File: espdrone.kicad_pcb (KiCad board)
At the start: 6 copper layers, 55 x 55 mm, 517 parts, among them J1 Conn_02x03_Odd_Even, J10 Conn_01x04_Pin, J11 Conn_01x04_Pin, J2 Conn_01x02, J3 Conn_01x14, J4 Conn_Coaxial, J5 Conn_01x04_Pin, J6 Conn_01x04, J7 Conn_01x06, J8 Conn_01x04_Pin, J9 Conn_01x04_Pin, Q1 NMOS, Q10 PSMN1R4-40YLDX, Q11 PSMN1R4-40YLDX, Q12 PSMN1R4-40YLDX, Q13 PSMN1R4-40YLDX, Q14 PSMN1R4-40YLDX, Q15 PSMN1R4-40YLDX, Q16 PSMN1R4-40YLDX, Q17 PSMN1R4-40YLDX, Q18 PSMN1R4-40YLDX, Q19 PSMN1R4-40YLDX, Q2 NMOS, Q20 PSMN1R4-40YLDX, Q21 PSMN1R4-40YLDX, Q22 PSMN1R4-40YLDX, Q23 PSMN1R4-40YLDX, Q24 PSMN1R4-40YLDX, Q25 PSMN1R4-40YLDX, Q26 PSMN1R4-40YLDX, Q27 PSMN1R4-40YLDX, Q28 PSMN1R4-40YLDX, Q3 NMOS, Q4 NMOS, Q5 PSMN1R4-40YLDX, Q6 PSMN1R4-40YLDX, Q7 PSMN1R4-40YLDX, Q8 PSMN1R4-40YLDX, Q9 PSMN1R4-40YLDX, U10 INA180A2, U11 FPC-1.0FX-15PWCR-H20, U12 VL53L1CXV0FY1, U13 LIS2MDL, U14 LSM6DS3, U15 PMW3901MB-TXQT_C43496881, U16 STM32G071K8U6, U17 DRV8328ARUYR, U18 INA180A2, U19 STM32G071K8U6, U2 USBLC6-2P6, U20 DRV8328ARUYR, U21 INA180A2, U22 STM32G071K8U6, U23 DRV8328ARUYR, U24 INA180A2, U25 STM32G071K8U6, U26 DRV8328ARUYR, U27 INA180A2, U3 W25Q128JVP, U4 LFD182G45DCHD277, U5 ESP32-C5HF4, U6 TLV62569DBV, U7 XC6206P182MR_C347373, U8 TPS63070RNMR, U9 TPS2121RUXR, Y1 Crystal_GND24, Y2 Crystal_GND24

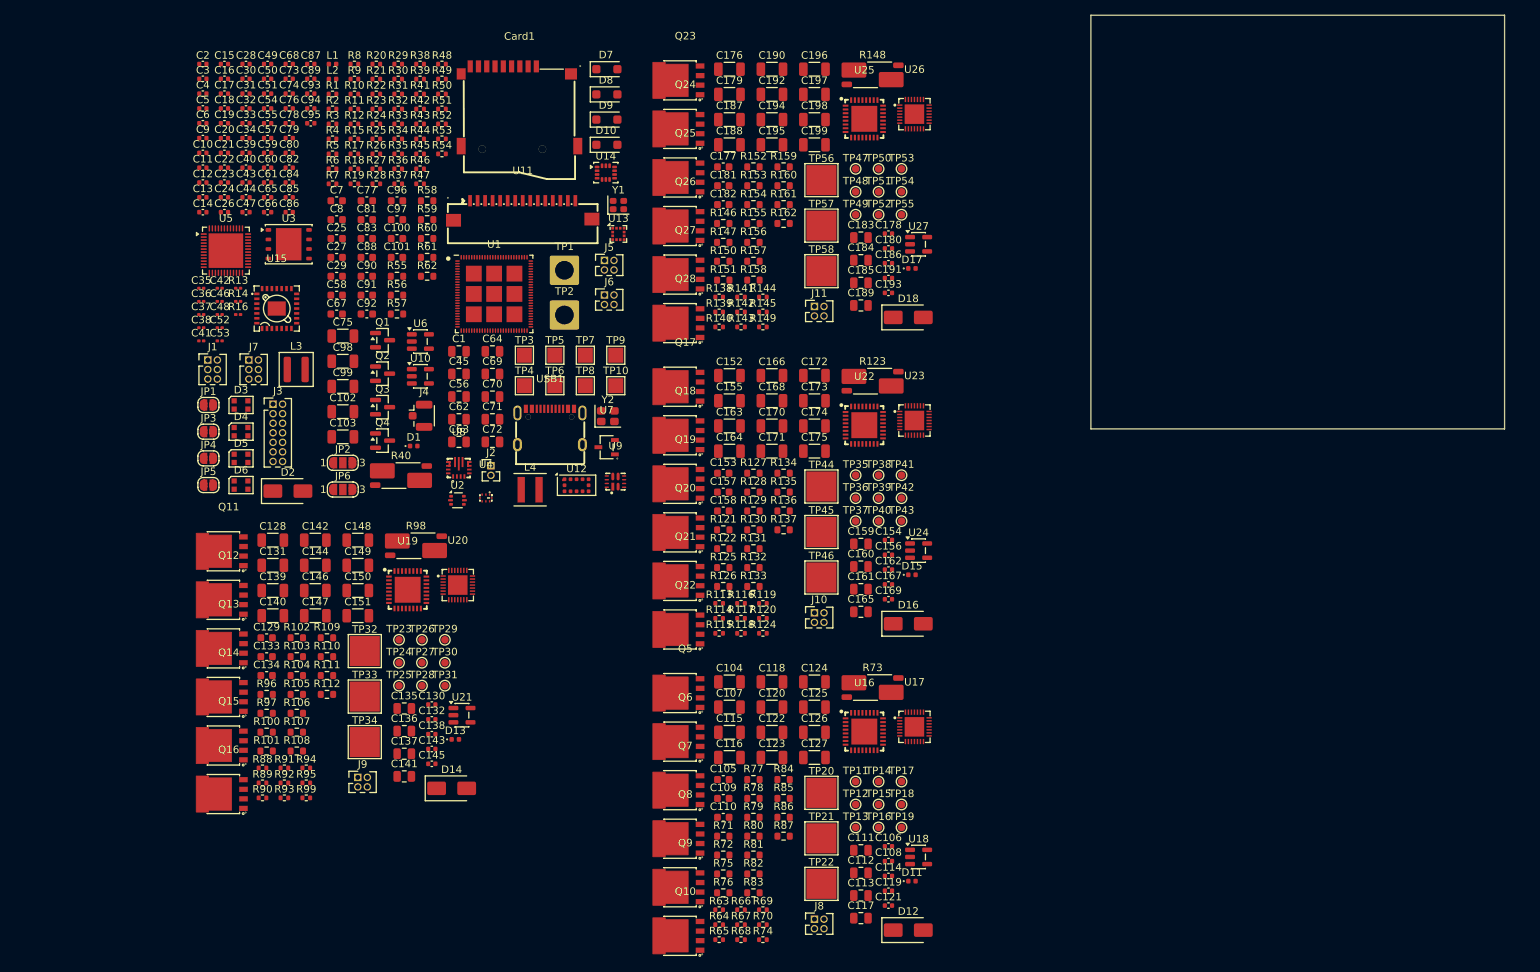
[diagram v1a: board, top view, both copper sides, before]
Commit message: Remove whole battery current shunt and replace MOSFETs with 3.3x3.3mm alternative
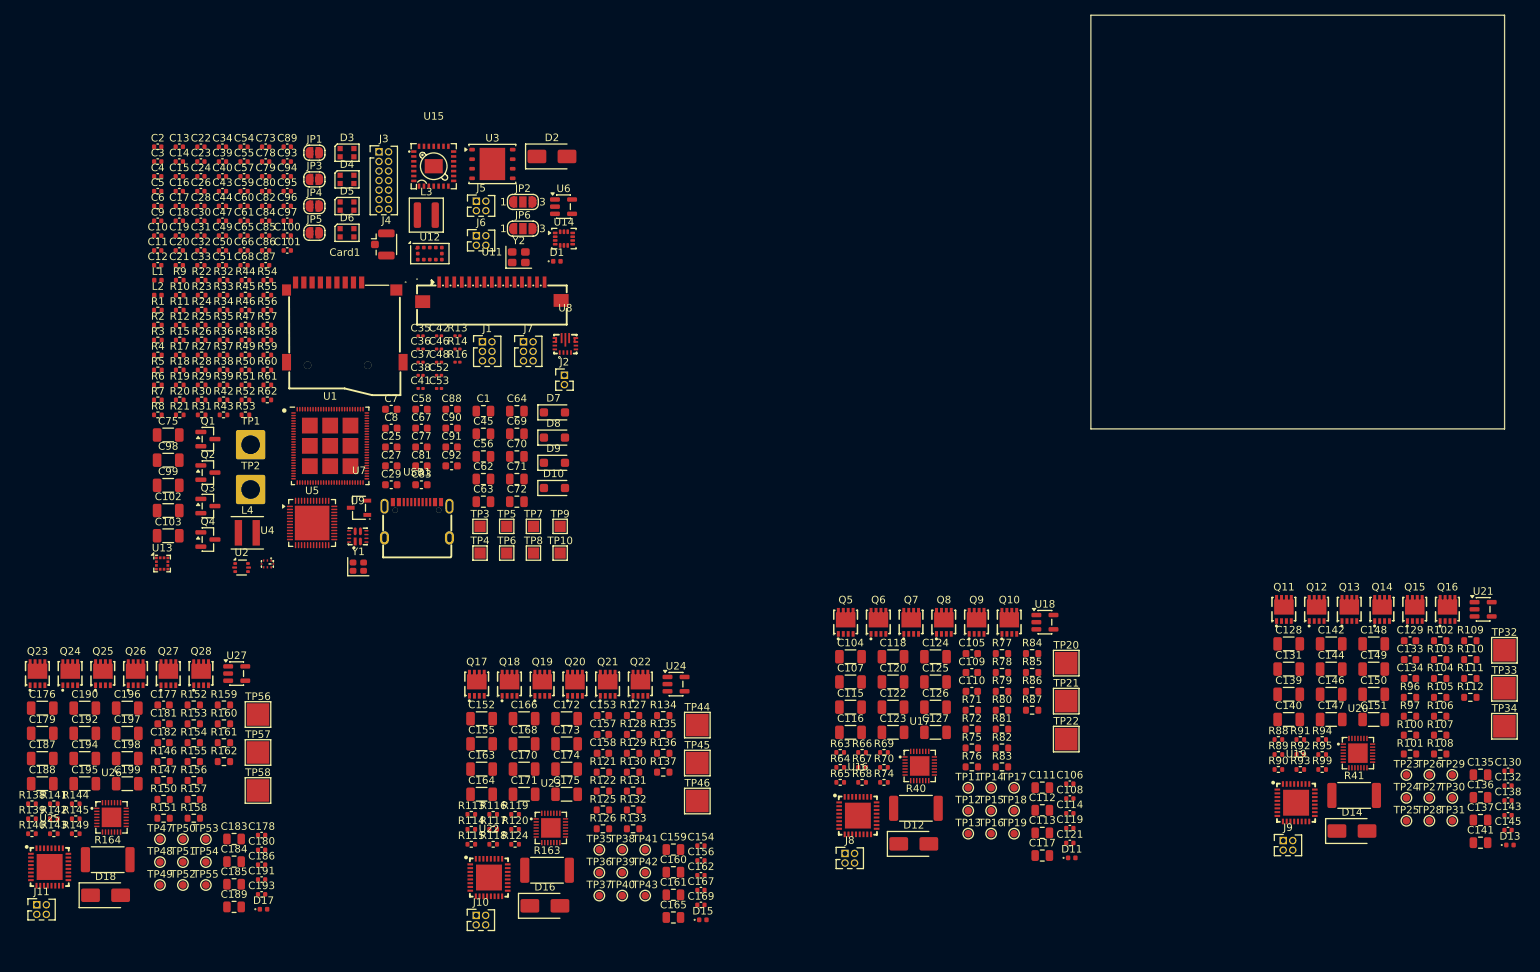
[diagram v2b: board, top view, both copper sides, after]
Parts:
- removed C74: 1n, Capacitor_SMD:C_0402_1005Metric
- removed C76: 100n, Capacitor_SMD:C_0402_1005Metric
- removed R123, R148, R73, R98: 0.001, Resistor_SMD:R_Shunt_Vishay_WSK2512_6332Metric_T2.66mm
- removed U10: INA180A2, Package_TO_SOT_SMD:SOT-23-5
- added R163: 0.001, Resistor_SMD:R_2512_6332Metric, F.Cu at (99.7, 147.7)
- added R164: 0.001, Resistor_SMD:R_2512_6332Metric, F.Cu at (41.3, 146.3)
- C100, C101, C96, C97: footprint Capacitor_SMD:C_0603_1608Metric -> Capacitor_SMD:C_0402_1005Metric
- Q10, Q11, Q12, Q13, Q14, Q15, Q16, Q17, Q18, Q19, Q20, Q21, Q22, Q23, Q24, Q25, Q26, Q27, Q28, Q5, Q6, Q7, Q8, Q9: value PSMN1R4-40YLDX -> NMOS; footprint easyeda2kicad:SOT-669_L4.9-W4.0-P1.27-LS6.0-BR -> easyeda2kicad:PDFN3333-8_L3.1-W3.2-P0.65-LS3.4-BL
- R100, R125, R150, R75: value 10k -> 10
- R101, R126, R151, R76: value 1k -> 10
- R102, R127, R152, R77: value 10 -> 10k
- R103, R128, R153, R78: value 10 -> 1k
- R40: value 0.0005 -> 0.001; footprint Resistor_SMD:R_Shunt_Vishay_WSK2512_6332Metric_T2.66mm -> Resistor_SMD:R_2512_6332Metric
- R41: value 1k -> 0.001; footprint Resistor_SMD:R_0402_1005Metric -> Resistor_SMD:R_2512_6332Metric
- R55, R56, R57, R58, R59, R60, R61, R62: footprint Resistor_SMD:R_0603_1608Metric -> Resistor_SMD:R_0402_1005Metric
- TP10, TP3, TP4, TP5, TP6, TP7, TP8, TP9: footprint TestPoint:TestPoint_Pad_2.0x2.0mm -> TestPoint:TestPoint_Pad_1.5x1.5mm
- TP20, TP21, TP22, TP32, TP33, TP34, TP44, TP45, TP46, TP56, TP57, TP58: footprint TestPoint:TestPoint_Pad_4.0x4.0mm -> TestPoint:TestPoint_Pad_3.0x3.0mm
- moved Q16 163.9 mm to (219.4, 113.0)
- moved Q15 158.7 mm to (215.1, 113.0)
- moved R41 155.3 mm to (207.0, 137.7)
- moved Q14 153.8 mm to (210.7, 113.0)
- moved C129 152.0 mm to (214.4, 117.2)
- moved C133 152.0 mm to (214.4, 119.7)
- moved C134 152.0 mm to (214.4, 122.2)
- moved R100 152.0 mm to (214.4, 129.7)
- moved R101 152.0 mm to (214.4, 132.2)
- moved R96 152.0 mm to (214.4, 124.7)
- moved R97 152.0 mm to (214.4, 127.2)
- moved R102 152.0 mm to (218.4, 117.2)
- moved R103 152.0 mm to (218.4, 119.7)
- moved R104 152.0 mm to (218.4, 122.2)
- moved R105 152.0 mm to (218.4, 124.7)
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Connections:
- C75 pad 2: Net-(C75-Pad2) -> +BATT
- Q10 pad 1: /Motors/ESC/LSS -> Net-(Q10-D)
- Q10 pad 2: /Motors/ESC/LSS -> Net-(Q10-G)
- Q11 pad 1: Net-(Q12-D) -> +BATT
- Q11 pad 2: /Motors/ESC1/A -> Net-(Q11-G)
- Q11 pad 3: /Motors/ESC1/A -> Net-(Q11-S)
- Q12 pad 1: /Motors/ESC1/LSS -> Net-(Q11-S)
- Q12 pad 2: /Motors/ESC1/LSS -> Net-(Q12-G)
- Q13 pad 1: Net-(Q14-D) -> +BATT
- Q13 pad 2: /Motors/ESC1/B -> Net-(Q13-G)
- Q13 pad 3: /Motors/ESC1/B -> Net-(Q13-S)
- Q14 pad 1: /Motors/ESC1/LSS -> Net-(Q13-S)
- Q14 pad 2: /Motors/ESC1/LSS -> Net-(Q14-G)
- Q15 pad 1: Net-(Q16-D) -> +BATT
- Q15 pad 2: /Motors/ESC1/C -> Net-(Q15-G)
- Q15 pad 3: /Motors/ESC1/C -> Net-(Q15-S)
- Q16 pad 1: /Motors/ESC1/LSS -> Net-(Q15-S)
- Q16 pad 2: /Motors/ESC1/LSS -> Net-(Q16-G)
- Q17 pad 1: Net-(Q18-D) -> +BATT
- Q17 pad 2: /Motors/ESC2/A -> Net-(Q17-G)
- Q17 pad 3: /Motors/ESC2/A -> Net-(Q17-S)
- Q18 pad 1: /Motors/ESC2/LSS -> Net-(Q17-S)
- Q18 pad 2: /Motors/ESC2/LSS -> Net-(Q18-G)
- Q19 pad 1: Net-(Q20-D) -> +BATT
- Q19 pad 2: /Motors/ESC2/B -> Net-(Q19-G)
- Q19 pad 3: /Motors/ESC2/B -> Net-(Q19-S)
- Q20 pad 1: /Motors/ESC2/LSS -> Net-(Q19-S)
- Q20 pad 2: /Motors/ESC2/LSS -> Net-(Q20-G)
- Q21 pad 1: Net-(Q22-D) -> +BATT
- Q21 pad 2: /Motors/ESC2/C -> Net-(Q21-G)
- Q21 pad 3: /Motors/ESC2/C -> Net-(Q21-S)
- Q22 pad 1: /Motors/ESC2/LSS -> Net-(Q21-S)
- Q22 pad 2: /Motors/ESC2/LSS -> Net-(Q22-G)
- Q23 pad 1: Net-(Q24-D) -> +BATT
- Q23 pad 2: /Motors/ESC3/A -> Net-(Q23-G)
- Q23 pad 3: /Motors/ESC3/A -> Net-(Q23-S)
- Q24 pad 1: /Motors/ESC3/LSS -> Net-(Q23-S)
- Q24 pad 2: /Motors/ESC3/LSS -> Net-(Q24-G)
- Q25 pad 1: Net-(Q26-D) -> +BATT
- Q25 pad 2: /Motors/ESC3/B -> Net-(Q25-G)
- Q25 pad 3: /Motors/ESC3/B -> Net-(Q25-S)
- Q26 pad 1: /Motors/ESC3/LSS -> Net-(Q25-S)
- Q26 pad 2: /Motors/ESC3/LSS -> Net-(Q26-G)
- Q27 pad 1: Net-(Q28-D) -> +BATT
- Q27 pad 2: /Motors/ESC3/C -> Net-(Q27-G)
- Q27 pad 3: /Motors/ESC3/C -> Net-(Q27-S)
- Q28 pad 1: /Motors/ESC3/LSS -> Net-(Q27-S)
- Q28 pad 2: /Motors/ESC3/LSS -> Net-(Q28-G)
- Q5 pad 1: Net-(Q6-D) -> +BATT
- Q5 pad 2: /Motors/ESC/A -> Net-(Q5-G)
- Q5 pad 3: /Motors/ESC/A -> Net-(Q5-S)
- Q6 pad 1: /Motors/ESC/LSS -> Net-(Q5-S)
- Q6 pad 2: /Motors/ESC/LSS -> Net-(Q6-G)
- Q7 pad 1: Net-(Q8-D) -> +BATT
- Q7 pad 2: /Motors/ESC/B -> Net-(Q7-G)
- Q7 pad 3: /Motors/ESC/B -> Net-(Q7-S)
- Q8 pad 1: /Motors/ESC/LSS -> Net-(Q7-S)
- Q8 pad 2: /Motors/ESC/LSS -> Net-(Q8-G)
- Q9 pad 1: Net-(Q10-D) -> +BATT
- Q9 pad 2: /Motors/ESC/C -> Net-(Q9-G)
- Q9 pad 3: /Motors/ESC/C -> Net-(Q10-D)
- R100 pad 1: /Motors/ESC1/VSENSE_A -> Net-(Q13-G)
- R100 pad 2: /Motors/ESC1/VSENSE_REF -> /Motors/ESC1/GHB
- R101 pad 1: GND -> Net-(Q14-G)
- R101 pad 2: /Motors/ESC1/VSENSE_A -> /Motors/ESC1/GLB
- R102 pad 1: Net-(Q13-G) -> /Motors/ESC1/VSENSE_A
- R102 pad 2: /Motors/ESC1/GHB -> /Motors/ESC1/VSENSE_REF
- R103 pad 1: Net-(Q14-G) -> GND
- R103 pad 2: /Motors/ESC1/GLB -> /Motors/ESC1/VSENSE_A
- R125 pad 1: /Motors/ESC2/VSENSE_A -> Net-(Q19-G)
- R125 pad 2: /Motors/ESC2/VSENSE_REF -> /Motors/ESC2/GHB
- R126 pad 1: GND -> Net-(Q20-G)
- R126 pad 2: /Motors/ESC2/VSENSE_A -> /Motors/ESC2/GLB
- R127 pad 1: Net-(Q19-G) -> /Motors/ESC2/VSENSE_A
- R127 pad 2: /Motors/ESC2/GHB -> /Motors/ESC2/VSENSE_REF
- R128 pad 1: Net-(Q20-G) -> GND
- R128 pad 2: /Motors/ESC2/GLB -> /Motors/ESC2/VSENSE_A
- R150 pad 1: /Motors/ESC3/VSENSE_A -> Net-(Q25-G)
- R150 pad 2: /Motors/ESC3/VSENSE_REF -> /Motors/ESC3/GHB
- R151 pad 1: GND -> Net-(Q26-G)
- R151 pad 2: /Motors/ESC3/VSENSE_A -> /Motors/ESC3/GLB
- R152 pad 1: Net-(Q25-G) -> /Motors/ESC3/VSENSE_A
- R152 pad 2: /Motors/ESC3/GHB -> /Motors/ESC3/VSENSE_REF
- R153 pad 1: Net-(Q26-G) -> GND
- R153 pad 2: /Motors/ESC3/GLB -> /Motors/ESC3/VSENSE_A
- R40 pad 1: +BATT -> /Motors/ESC/LSS
- R40 pad 2: Net-(U10--) -> GND
- R41 pad 1: BAT_ISENSE -> /Motors/ESC1/LSS
- R41 pad 2: Net-(R41-Pad2) -> GND
- R75 pad 1: /Motors/ESC/VSENSE_A -> Net-(Q7-G)
- R75 pad 2: /Motors/ESC/VSENSE_REF -> /Motors/ESC/GHB
- R76 pad 1: GND -> Net-(Q8-G)
- R76 pad 2: /Motors/ESC/VSENSE_A -> /Motors/ESC/GLB
- R77 pad 1: Net-(Q7-G) -> /Motors/ESC/VSENSE_A
- R77 pad 2: /Motors/ESC/GHB -> /Motors/ESC/VSENSE_REF
- R78 pad 1: Net-(Q8-G) -> GND
- R78 pad 2: /Motors/ESC/GLB -> /Motors/ESC/VSENSE_A
- TP1 pad 1: Net-(C75-Pad2) -> +BATT
- U18 pad 3: Net-(U18-+) -> /Motors/ESC/LSS
- U18 pad 4: Net-(U18--) -> GND
- U21 pad 3: Net-(U21-+) -> /Motors/ESC1/LSS
- U21 pad 4: Net-(U21--) -> GND
- U24 pad 3: Net-(U24-+) -> /Motors/ESC2/LSS
- U24 pad 4: Net-(U24--) -> GND
- U27 pad 3: Net-(U27-+) -> /Motors/ESC3/LSS
- U27 pad 4: Net-(U27--) -> GND

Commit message: Improve some connector footprints
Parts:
- removed C198, C199: 10u, Capacitor_SMD:C_1206_3216Metric
- removed D15, D17: LED, LED_SMD:LED_0402_1005Metric
- removed D16, D18: SMAJ14A, Diode_SMD:D_SMA
- removed J6: Conn_01x04, Connector_PinHeader_1.27mm:PinHeader_2x02_P1.27mm_Vertical
- removed R161: 1k, Resistor_SMD:R_0603_1608Metric
- removed R162: 10k, Resistor_SMD:R_0603_1608Metric
- removed R163, R164: 0.001, Resistor_SMD:R_2512_6332Metric
- removed U27: INA180A2, Package_TO_SOT_SMD:SOT-23-5
- added C74: 100u, Capacitor_SMD:C_1206_3216Metric, F.Cu at (329.4, 5.06)
- added C76: 100n, Capacitor_SMD:C_0402_1005Metric, F.Cu at (214.2, 28.3)
- added J12: Conn_01x04, easyeda2kicad:Connector_Pad_1.27mm_1x04, F.Cu at (252.8, 67.5)
- added R123: 10, Resistor_SMD:R_0603_1608Metric, F.Cu at (315.1, -26.3)
- added R148: 10, Resistor_SMD:R_0603_1608Metric, F.Cu at (360.1, -25.3)
- added R73: 10, Resistor_SMD:R_0603_1608Metric, F.Cu at (271.6, -27.3)
- added R98: 10, Resistor_SMD:R_0603_1608Metric, F.Cu at (225.0, -28.3)
- added U10: FPC-1.0FX-15PWCR-H20, easyeda2kicad:FPC-SMD_15P-P1.00_XUNPU_FPC-1.0FX-15PWCR-H20, F.Cu at (244.3, 45.6)
- C100, C101, C96, C97: value 100n -> 100u; footprint Capacitor_SMD:C_0402_1005Metric -> Capacitor_SMD:C_1206_3216Metric
- C102: value 100u -> 10u
- C103: value 100u -> 100n; footprint Capacitor_SMD:C_1206_3216Metric -> Capacitor_SMD:C_0603_1608Metric
- C104, C128, C152, C176: value 10u -> 100n; footprint Capacitor_SMD:C_1206_3216Metric -> Capacitor_SMD:C_0402_1005Metric
- C105, C129, C153, C177: value 100n -> 10u; footprint Capacitor_SMD:C_0603_1608Metric -> Capacitor_SMD:C_1206_3216Metric
- C107, C131, C155, C179: value 10u -> 470nF; footprint Capacitor_SMD:C_1206_3216Metric -> Capacitor_SMD:C_0603_1608Metric
- C108, C132, C156, C180, C79: value 100n -> 1u; footprint Capacitor_SMD:C_0402_1005Metric -> Capacitor_SMD:C_0603_1608Metric
- C109, C133, C157, C181: value 470nF -> 1u; footprint Capacitor_SMD:C_0603_1608Metric -> Capacitor_SMD:C_0805_2012Metric
- C110, C134, C158, C182: footprint Capacitor_SMD:C_0603_1608Metric -> Capacitor_SMD:C_0805_2012Metric
- C112, C117, C136, C141, C160, C165, C184, C189: value 1u -> 100n; footprint Capacitor_SMD:C_0805_2012Metric -> Capacitor_SMD:C_0402_1005Metric
- C113, C137, C161, C185: value 1u -> 10u; footprint Capacitor_SMD:C_0805_2012Metric -> Capacitor_SMD:C_1206_3216Metric
- C114, C138, C162, C186: value 100n -> 10u; footprint Capacitor_SMD:C_0402_1005Metric -> Capacitor_SMD:C_1206_3216Metric
- C115, C139, C163, C187: value 10u -> 1u; footprint Capacitor_SMD:C_1206_3216Metric -> Capacitor_SMD:C_0805_2012Metric
- C119, C143, C167, C191: value 100n -> 1n
- C121, C145, C169, C193: value 1n -> 10u; footprint Capacitor_SMD:C_0402_1005Metric -> Capacitor_SMD:C_1206_3216Metric
- C127, C151, C175: value 10u -> 100n; footprint Capacitor_SMD:C_1206_3216Metric -> Capacitor_SMD:C_0603_1608Metric
- C35, C36: value TBD -> 12pF; footprint Capacitor_SMD:C_0201_0603Metric -> Capacitor_SMD:C_0402_1005Metric
- C37, C38, C41: value TBD -> 1u; footprint Capacitor_SMD:C_0201_0603Metric -> Capacitor_SMD:C_0402_1005Metric
- C39: value 12pF -> 10u; footprint Capacitor_SMD:C_0402_1005Metric -> Capacitor_SMD:C_0805_2012Metric
- C40: value 12pF -> 0.8p; footprint Capacitor_SMD:C_0402_1005Metric -> Capacitor_SMD:C_0201_0603Metric
- C42: value TBD -> 0.3p
- C43, C44, C51: value 1u -> 100n
- C45: value 10u -> 1u; footprint Capacitor_SMD:C_0805_2012Metric -> Capacitor_SMD:C_0402_1005Metric
- C46: value 0.8p -> 2.6p
- C47: value 1u -> 3p; footprint Capacitor_SMD:C_0402_1005Metric -> Capacitor_SMD:C_0201_0603Metric
- C48: value 0.3p -> 100n; footprint Capacitor_SMD:C_0201_0603Metric -> Capacitor_SMD:C_0402_1005Metric
- C49: value 100n -> 10n
- C50: value 100n -> 10u; footprint Capacitor_SMD:C_0402_1005Metric -> Capacitor_SMD:C_0805_2012Metric
- C52: value 2.6p -> TBD
- C53: value 3p -> TBD
- C54, C57: value 100n -> TBD; footprint Capacitor_SMD:C_0402_1005Metric -> Capacitor_SMD:C_0201_0603Metric
- C55: value 10n -> TBD; footprint Capacitor_SMD:C_0402_1005Metric -> Capacitor_SMD:C_0201_0603Metric
- C56: value 10u -> TBD; footprint Capacitor_SMD:C_0805_2012Metric -> Capacitor_SMD:C_0201_0603Metric
- C75: value 100u -> 10u; footprint Capacitor_SMD:C_1206_3216Metric -> Capacitor_SMD:C_0603_1608Metric
- C77, C92: value 10u -> 100n; footprint Capacitor_SMD:C_0603_1608Metric -> Capacitor_SMD:C_0402_1005Metric
- C81: value 1u -> 4.7u
- C83: value 4.7u -> 10n; footprint Capacitor_SMD:C_0603_1608Metric -> Capacitor_SMD:C_0402_1005Metric
- C85: value 10n -> 220n
- C86: value 100n -> 10u; footprint Capacitor_SMD:C_0402_1005Metric -> Capacitor_SMD:C_0603_1608Metric
- C87: value 220n -> 100n
- C89: value 100n -> 4.7u; footprint Capacitor_SMD:C_0402_1005Metric -> Capacitor_SMD:C_0603_1608Metric
- C91: value 4.7u -> 100n; footprint Capacitor_SMD:C_0603_1608Metric -> Capacitor_SMD:C_0402_1005Metric
- C98, C99: value 100u -> 100n; footprint Capacitor_SMD:C_1206_3216Metric -> Capacitor_SMD:C_0402_1005Metric
- D12, D14: value SMAJ14A -> LED; footprint Diode_SMD:D_SMA -> LED_SMD:LED_0402_1005Metric
- D2: value SMAJ14A -> SMF14A; footprint Diode_SMD:D_SMA -> Diode_SMD:D_SMF
- J1: value Conn_02x03_Odd_Even -> Conn_01x06; footprint Connector_PinHeader_1.27mm:PinHeader_2x03_P1.27mm_Vertical -> easyeda2kicad:Connector_Pad_1.27mm_1x06
- J10, J11, J8, J9: value Conn_01x04_Pin -> Conn_01x04; footprint Connector_PinHeader_1.27mm:PinHeader_2x02_P1.27mm_Vertical -> easyeda2kicad:Connector_Pad_1.27mm_1x04
- J2: value Conn_01x02 -> Conn_01x04; footprint Connector_PinHeader_1.27mm:PinHeader_1x02_P1.27mm_Vertical -> easyeda2kicad:Connector_Pad_1.27mm_1x04
- J3: footprint Connector_PinHeader_1.27mm:PinHeader_2x07_P1.27mm_Vertical -> easyeda2kicad:Connector_pad_1.27mm_2x07
- J4: value Conn_Coaxial -> Conn_01x06; footprint Connector_Coaxial:U.FL_Hirose_U.FL-R-SMT-1_Vertical -> easyeda2kicad:Connector_Pad_1.27mm_1x06
- J5: value Conn_01x04_Pin -> Conn_Coaxial; footprint Connector_PinHeader_1.27mm:PinHeader_2x02_P1.27mm_Vertical -> Connector_Coaxial:U.FL_Hirose_U.FL-R-SMT-1_Vertical
- J7: footprint Connector_PinHeader_1.27mm:PinHeader_2x03_P1.27mm_Vertical -> easyeda2kicad:Connector_Pad_1.27mm_1x06
- R100, R108, R125, R133, R150, R158, R55, R56, R59, R60, R75, R83: value 10 -> 10k
- R101, R109, R126, R134, R151, R159, R76, R84: value 10 -> 1k
- R103, R116, R128, R141, R153, R66, R78, R91: value 1k -> 10k
- R104, R118, R129, R143, R154, R68, R79, R93: value 10k -> 1k
- R106, R131, R156, R81: value 1k -> 10
- R107, R132, R157, R53, R57, R58, R82: value 10k -> 10
- R111, R136, R86: value 1k -> 4.7k; footprint Resistor_SMD:R_0603_1608Metric -> Resistor_SMD:R_0402_1005Metric
- R112, R137, R87: value 10k -> 4.7k; footprint Resistor_SMD:R_0603_1608Metric -> Resistor_SMD:R_0402_1005Metric
- R113, R138, R63, R88: value 4.7k -> 10k
- R114, R139, R64, R89: value 4.7k -> 1k
- R115, R140, R65, R90: value 10k -> 220k
- R117, R142, R67, R92: value 220k -> 10k
- R119, R144, R69, R94: value 10k -> 10; footprint Resistor_SMD:R_0402_1005Metric -> Resistor_SMD:R_0603_1608Metric
- R120, R124, R145, R149, R70, R74, R95, R99: value 1k -> 10; footprint Resistor_SMD:R_0402_1005Metric -> Resistor_SMD:R_0603_1608Metric
- R121, R146, R71, R96: value 10 -> 0.001; footprint Resistor_SMD:R_0603_1608Metric -> Resistor_SMD:R_2512_6332Metric
- R122, R147, R72, R97: value 10 -> 1k; footprint Resistor_SMD:R_0603_1608Metric -> Resistor_SMD:R_0402_1005Metric
- R13, R14: value 0 -> 10k; footprint Resistor_SMD:R_0201_0603Metric -> Resistor_SMD:R_0402_1005Metric
- R16: value 0 -> 47k; footprint Resistor_SMD:R_0201_0603Metric -> Resistor_SMD:R_0402_1005Metric
- R17, R23, R25: value 10k -> 47k
- R20, R22, R45, R46: value 47k -> 10k
- R26, R28: value 47k -> 0; footprint Resistor_SMD:R_0402_1005Metric -> Resistor_SMD:R_0201_0603Metric
- R27: value 10k -> 0; footprint Resistor_SMD:R_0402_1005Metric -> Resistor_SMD:R_0201_0603Metric
- R40, R41: value 0.001 -> 47k; footprint Resistor_SMD:R_2512_6332Metric -> Resistor_SMD:R_0402_1005Metric
- R52, R61, R62: value 10k -> 4.7k
- R54: value 4.7k -> 10
- TP1, TP2: footprint Connector_Wire:SolderWire-2sqmm_1x01_D2mm_OD3.9mm -> easyeda2kicad:BatteryPad_4x3mm
- TP10, TP3, TP4, TP5, TP6, TP7, TP8, TP9: footprint TestPoint:TestPoint_Pad_1.5x1.5mm -> easyeda2kicad:MotorPad_1x3mm
- TP20, TP21, TP22, TP32, TP33, TP34, TP44, TP45, TP46, TP56, TP57, TP58: footprint TestPoint:TestPoint_Pad_3.0x3.0mm -> easyeda2kicad:MotorPad_1x3mm
- U11: value FPC-1.0FX-15PWCR-H20 -> VL53L1CXV0FY1; footprint easyeda2kicad:FPC-SMD_15P-P1.00_XUNPU_FPC-1.0FX-15PWCR-H20 -> Sensor_Distance:ST_VL53L1x
- U12: value VL53L1CXV0FY1 -> LIS2MDL; footprint Sensor_Distance:ST_VL53L1x -> Package_LGA:LGA-12_2x2mm_P0.5mm
- U13: value LIS2MDL -> LSM6DS3; footprint Package_LGA:LGA-12_2x2mm_P0.5mm -> Package_LGA:LGA-14_3x2.5mm_P0.5mm_LayoutBorder3x4y
- U14: value LSM6DS3 -> PMW3901MB-TXQT_C43496881; footprint Package_LGA:LGA-14_3x2.5mm_P0.5mm_LayoutBorder3x4y -> lcsc_footprints:C43496881_COB-28_L6_0-W6_0-P0_65-TL-EP
- U15: value PMW3901MB-TXQT_C43496881 -> STM32G071K8U6; footprint lcsc_footprints:C43496881_COB-28_L6_0-W6_0-P0_65-TL-EP -> easyeda2kicad:UFQFPN-32_L5.0-W5.0-P0.50-TL-EP3.5
- U16, U19, U22, U25: value STM32G071K8U6 -> DRV8328ARUYR; footprint easyeda2kicad:UFQFPN-32_L5.0-W5.0-P0.50-TL-EP3.5 -> easyeda2kicad:QFN-28_L4.0-W4.0-P0.40-BL-EP2.6
- U17, U20, U23, U26: value DRV8328ARUYR -> INA180A2; footprint easyeda2kicad:QFN-28_L4.0-W4.0-P0.40-BL-EP2.6 -> Package_TO_SOT_SMD:SOT-23-5
- U18, U21, U24: value INA180A2 -> STM32G071K8U6; footprint Package_TO_SOT_SMD:SOT-23-5 -> easyeda2kicad:UFQFPN-32_L5.0-W5.0-P0.50-TL-EP3.5
- U4: value LFD182G45DCHD277 -> ESP32-C5HF4; footprint easyeda2kicad:FILTER-SMD_8P-L1.6-W0.8-LFD182G45DCHD277 -> Package_DFN_QFN:QFN-48-1EP_6x6mm_P0.4mm_EP4.6x4.6mm
- U5: value ESP32-C5HF4 -> LFD182G45DCHD277; footprint Package_DFN_QFN:QFN-48-1EP_6x6mm_P0.4mm_EP4.6x4.6mm -> easyeda2kicad:FILTER-SMD_8P-L1.6-W0.8-LFD182G45DCHD277
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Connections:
- C104 pad 1: +BATT -> GND
- C104 pad 2: GND -> +3V3
- C105 pad 1: +BATT -> /Motors/ESC1/GVDD
- C107 pad 1: /Motors/ESC/GVDD -> Net-(U16-CPL)
- C107 pad 2: GND -> Net-(U16-CPH)
- C109 pad 1: Net-(U17-CPL) -> /Motors/ESC1/A
- C109 pad 2: Net-(U17-CPH) -> /Motors/ESC1/BSTA
- C110 pad 1: GND -> /Motors/ESC1/B
- C110 pad 2: +3V3 -> Net-(U16-BSTB)
- C111 pad 1: /Motors/ESC/A -> /Motors/ESC1/C
- C111 pad 2: /Motors/ESC/BSTA -> Net-(U16-BSTC)
- C112 pad 1: /Motors/ESC/B -> GND
- C112 pad 2: Net-(U17-BSTB) -> +BATT
- C113 pad 1: /Motors/ESC/C -> GND
- C113 pad 2: Net-(U17-BSTC) -> +BATT
- C117 pad 1: GND -> +3V3
- C117 pad 2: +BATT -> GND
- C119 pad 1: +3V3 -> /Motors/ESC1/ISENSE
- C121 pad 1: /Motors/ESC/ISENSE -> GND
- C121 pad 2: GND -> +BATT
- C126 pad 1: GND -> +BATT
- C126 pad 2: +BATT -> GND
- C127 pad 1: GND -> +BATT
- C127 pad 2: +BATT -> GND
- C128 pad 1: +BATT -> GND
- C128 pad 2: GND -> +3V3
- C129 pad 1: +BATT -> /Motors/ESC2/GVDD
- C131 pad 1: /Motors/ESC1/GVDD -> Net-(U19-CPL)
- C131 pad 2: GND -> Net-(U19-CPH)
- C133 pad 1: Net-(U20-CPL) -> /Motors/ESC2/A
- C133 pad 2: Net-(U20-CPH) -> /Motors/ESC2/BSTA
- C134 pad 1: GND -> /Motors/ESC2/B
- C134 pad 2: +3V3 -> Net-(U19-BSTB)
- C135 pad 1: /Motors/ESC1/A -> /Motors/ESC2/C
- C135 pad 2: /Motors/ESC1/BSTA -> Net-(U19-BSTC)
- C136 pad 1: /Motors/ESC1/B -> GND
- C136 pad 2: Net-(U20-BSTB) -> +BATT
- C137 pad 1: /Motors/ESC1/C -> GND
- C137 pad 2: Net-(U20-BSTC) -> +BATT
- C141 pad 1: GND -> +3V3
- C141 pad 2: +BATT -> GND
- C143 pad 1: +3V3 -> /Motors/ESC2/ISENSE
- C145 pad 1: /Motors/ESC1/ISENSE -> GND
- C145 pad 2: GND -> +BATT
- C150 pad 1: GND -> +BATT
- C150 pad 2: +BATT -> GND
- C151 pad 1: GND -> +BATT
- C151 pad 2: +BATT -> GND
- C152 pad 1: +BATT -> GND
- C152 pad 2: GND -> +3V3
- C153 pad 1: +BATT -> /Motors/ESC3/GVDD
- C155 pad 1: /Motors/ESC2/GVDD -> Net-(U22-CPL)
- C155 pad 2: GND -> Net-(U22-CPH)
- C157 pad 1: Net-(U23-CPL) -> /Motors/ESC3/A
- C157 pad 2: Net-(U23-CPH) -> /Motors/ESC3/BSTA
- C158 pad 1: GND -> /Motors/ESC3/B
- C158 pad 2: +3V3 -> Net-(U22-BSTB)
- C159 pad 1: /Motors/ESC2/A -> /Motors/ESC3/C
- C159 pad 2: /Motors/ESC2/BSTA -> Net-(U22-BSTC)
- C160 pad 1: /Motors/ESC2/B -> GND
- C160 pad 2: Net-(U23-BSTB) -> +BATT
- C161 pad 1: /Motors/ESC2/C -> GND
- C161 pad 2: Net-(U23-BSTC) -> +BATT
- C165 pad 1: GND -> +3V3
- C165 pad 2: +BATT -> GND
- C167 pad 1: +3V3 -> /Motors/ESC3/ISENSE
- C169 pad 1: /Motors/ESC2/ISENSE -> GND
- C169 pad 2: GND -> +BATT
- C174 pad 1: GND -> +BATT
- C174 pad 2: +BATT -> GND
- C175 pad 1: GND -> +BATT
- C175 pad 2: +BATT -> GND
- C176 pad 1: +BATT -> GND
- C176 pad 2: GND -> +3V3
- C177 pad 1: +BATT -> /Motors/ESC4/GVDD
- C179 pad 1: /Motors/ESC3/GVDD -> Net-(U25-CPL)
- C179 pad 2: GND -> Net-(U25-CPH)
- C181 pad 1: Net-(U26-CPL) -> /Motors/ESC4/A
- C181 pad 2: Net-(U26-CPH) -> /Motors/ESC4/BSTA
- C182 pad 1: GND -> /Motors/ESC4/B
- C182 pad 2: +3V3 -> Net-(U25-BSTB)
- C183 pad 1: /Motors/ESC3/A -> /Motors/ESC4/C
- C183 pad 2: /Motors/ESC3/BSTA -> Net-(U25-BSTC)
- C184 pad 1: /Motors/ESC3/B -> GND
- C184 pad 2: Net-(U26-BSTB) -> +BATT
- C185 pad 1: /Motors/ESC3/C -> GND
- C185 pad 2: Net-(U26-BSTC) -> +BATT
- C189 pad 1: GND -> +3V3
- C189 pad 2: +BATT -> GND
- C191 pad 1: +3V3 -> /Motors/ESC4/ISENSE
- C193 pad 1: /Motors/ESC3/ISENSE -> GND
- C193 pad 2: GND -> +BATT
- C35 pad 1: /Coprocessor/ANT_5G -> Net-(C35-Pad1)
- C36 pad 1: /Coprocessor/ANT_2G -> Net-(U4-XTAL_N)
- C37 pad 1: Net-(U4-P1) -> CP_EN
- C38 pad 1: Net-(U4-P2) -> +3V3
- C39 pad 1: Net-(C39-Pad1) -> +3V3
- C40 pad 1: Net-(U5-XTAL_N) -> +3V3
- C41 pad 1: Net-(U4-P3) -> +3V3
- C42 pad 1: Net-(J4-In) -> +3V3
- C43 pad 1: CP_EN -> +3V3
- C46 pad 1: +3V3 -> Net-(U4-VDDA1)
- C52 pad 1: Net-(U5-VDDA1) -> /Coprocessor/ANT_5G
- C53 pad 1: +3V3 -> /Coprocessor/ANT_2G
- C54 pad 1: +3V3 -> Net-(U5-P1)
- C55 pad 1: +3V3 -> Net-(U5-P2)
- C56 pad 1: +3V3 -> Net-(U5-P3)
- C57 pad 1: +3V3 -> Net-(J5-In)
- C75 pad 2: +BATT -> +3V3
- C77 pad 1: GND -> +3V3
- C77 pad 2: +3V3 -> GND
- C79 pad 1: +3V3 -> GND
- C79 pad 2: GND -> +3V3
- C82 pad 1: +3V3 -> GND
- C82 pad 2: GND -> +3V3
- C85 pad 2: +3V3 -> Net-(U12-C1)
- C87 pad 2: Net-(U13-C1) -> +3V3
- C88 pad 2: +3V3 -> +1V8
- C89 pad 2: +3V3 -> Net-(U14-VREG)
- C91 pad 2: Net-(U15-VREG) -> Net-(U14-VREG)
- C93 pad 2: Net-(U15-VREG) -> +3V3
- C94 pad 1: GND -> +BATT
- C94 pad 2: +1V8 -> GND
- C95 pad 1: GND -> +BATT
- C95 pad 2: +3V3 -> GND
- D12 pad 2: +BATT -> Net-(D12-A)
- D14 pad 2: +BATT -> Net-(D14-A)
- J1 pad 1: /MCU/P4_MTDO -> GND
- J1 pad 2: +3V3 -> /MCU/P4_MTDO
- J1 pad 3: GND -> /MCU/P4_MTMS
- J1 pad 4: /MCU/P4_MTCK -> /MCU/P4_MTDI
- J1 pad 5: /MCU/P4_MTMS -> /MCU/P4_MTCK
- J1 pad 6: /MCU/P4_MTDI -> +3V3
- J10 pad 1: +3V3 -> GND
- J10 pad 2: /Motors/ESC2/SWDIO -> /Motors/ESC3/SWCLK
- J10 pad 3: /Motors/ESC2/SWCLK -> /Motors/ESC3/SWDIO
- J10 pad 4: GND -> +3V3
- J11 pad 1: +3V3 -> GND
- J11 pad 2: /Motors/ESC3/SWDIO -> /Motors/ESC4/SWCLK
- J11 pad 3: /Motors/ESC3/SWCLK -> /Motors/ESC4/SWDIO
- J11 pad 4: GND -> +3V3
- J2 pad 1: Net-(J2-Pin_1) -> GND
- J3 pad 1: +3V3 -> GND
- J3 pad 10: /MCU/GPIO49 -> /MCU/GPIO30
- J3 pad 11: /MCU/GPIO50 -> /MCU/GPIO29
- J3 pad 12: /MCU/GPIO51 -> /MCU/GPIO28
- J3 pad 13: /MCU/GPIO52 -> /MCU/GPIO6
- J3 pad 14: GND -> +3V3
- J3 pad 2: /MCU/GPIO6 -> /MCU/GPIO52
- J3 pad 3: /MCU/GPIO28 -> /MCU/GPIO51
- J3 pad 4: /MCU/GPIO29 -> /MCU/GPIO50
- J3 pad 5: /MCU/GPIO30 -> /MCU/GPIO49
- J3 pad 6: /MCU/GPIO31 -> /MCU/GPIO34
- J3 pad 7: /MCU/GPIO32 -> /MCU/GPIO33
- J3 pad 8: /MCU/GPIO33 -> /MCU/GPIO32
- J3 pad 9: /MCU/GPIO34 -> /MCU/GPIO31
- J4 pad 1: Net-(J4-In) -> GND
- J4 pad 2: GND -> Net-(J4-Pin_2)
- J5 pad 1: Net-(J5-Pin_1) -> Net-(J5-In)
- J5 pad 2: Net-(J5-Pin_2) -> GND
- J7 pad 1: +3V3 -> GND
- J7 pad 2: SPI_CLK -> SPI_MOSI
- J7 pad 3: SPI_EXT_CS -> SPI_MISO
- J7 pad 4: SPI_MISO -> SPI_EXT_CS
- J7 pad 5: SPI_MOSI -> SPI_CLK
- J7 pad 6: GND -> +3V3
- J8 pad 1: +3V3 -> GND
- J8 pad 2: /Motors/ESC/SWDIO -> /Motors/ESC1/SWCLK
- J8 pad 3: /Motors/ESC/SWCLK -> /Motors/ESC1/SWDIO
- J8 pad 4: GND -> +3V3
- J9 pad 1: +3V3 -> GND
- J9 pad 2: /Motors/ESC1/SWDIO -> /Motors/ESC2/SWCLK
- J9 pad 3: /Motors/ESC1/SWCLK -> /Motors/ESC2/SWDIO
- J9 pad 4: GND -> +3V3
- JP2 pad 2: Net-(J5-Pin_2) -> Net-(J4-Pin_4)
- L1 pad 1: Net-(C39-Pad1) -> Net-(C35-Pad1)
- L1 pad 2: Net-(U5-XTAL_P) -> Net-(U4-XTAL_P)
- L2 pad 2: Net-(U5-VDDA1) -> Net-(U4-VDDA1)
- Q10 pad 3: /Motors/ESC/LSS -> /Motors/ESC1/LSS
- Q12 pad 3: /Motors/ESC1/LSS -> /Motors/ESC2/LSS
- Q14 pad 3: /Motors/ESC1/LSS -> /Motors/ESC2/LSS
- Q16 pad 3: /Motors/ESC1/LSS -> /Motors/ESC2/LSS
- Q18 pad 3: /Motors/ESC2/LSS -> /Motors/ESC3/LSS
- Q20 pad 3: /Motors/ESC2/LSS -> /Motors/ESC3/LSS
- Q22 pad 3: /Motors/ESC2/LSS -> /Motors/ESC3/LSS
- Q24 pad 3: /Motors/ESC3/LSS -> /Motors/ESC4/LSS
- Q26 pad 3: /Motors/ESC3/LSS -> /Motors/ESC4/LSS
- Q28 pad 3: /Motors/ESC3/LSS -> /Motors/ESC4/LSS
- Q6 pad 3: /Motors/ESC/LSS -> /Motors/ESC1/LSS
- Q8 pad 3: /Motors/ESC/LSS -> /Motors/ESC1/LSS
- R100 pad 1: Net-(Q13-G) -> /Motors/ESC2/VSENSE_A
- R100 pad 2: /Motors/ESC1/GHB -> /Motors/ESC2/VSENSE_REF
- R101 pad 1: Net-(Q14-G) -> GND
- R101 pad 2: /Motors/ESC1/GLB -> /Motors/ESC2/VSENSE_A
- R102 pad 1: /Motors/ESC1/VSENSE_A -> /Motors/ESC2/A
- R102 pad 2: /Motors/ESC1/VSENSE_REF -> /Motors/ESC2/VSENSE_A
- R103 pad 1: GND -> /Motors/ESC2/VSENSE_B
- R103 pad 2: /Motors/ESC1/VSENSE_A -> /Motors/ESC2/VSENSE_REF
- R104 pad 1: /Motors/ESC1/A -> GND
- R104 pad 2: /Motors/ESC1/VSENSE_A -> /Motors/ESC2/VSENSE_B
- R105 pad 1: /Motors/ESC1/VSENSE_B -> /Motors/ESC2/B
- R105 pad 2: /Motors/ESC1/VSENSE_REF -> /Motors/ESC2/VSENSE_B
- R106 pad 1: GND -> Net-(Q15-G)
- R106 pad 2: /Motors/ESC1/VSENSE_B -> /Motors/ESC2/GHC
- R107 pad 1: /Motors/ESC1/B -> Net-(Q16-G)
- R107 pad 2: /Motors/ESC1/VSENSE_B -> /Motors/ESC2/GLC
- R108 pad 1: Net-(Q15-G) -> /Motors/ESC2/VSENSE_C
- R108 pad 2: /Motors/ESC1/GHC -> /Motors/ESC2/VSENSE_REF
- R109 pad 1: Net-(Q16-G) -> GND
- R109 pad 2: /Motors/ESC1/GLC -> /Motors/ESC2/VSENSE_C
- R110 pad 1: /Motors/ESC1/VSENSE_C -> /Motors/ESC2/C
- R110 pad 2: /Motors/ESC1/VSENSE_REF -> /Motors/ESC2/VSENSE_C
- R111 pad 1: GND -> Net-(U21-PA0)
- R111 pad 2: /Motors/ESC1/VSENSE_C -> Net-(D13-A)
- R112 pad 1: /Motors/ESC1/C -> +3V3
- R112 pad 2: /Motors/ESC1/VSENSE_C -> /Motors/ESC3/NFAULT
- R113 pad 1: Net-(U22-PA0) -> Net-(U22-DT)
- R113 pad 2: Net-(D15-A) -> GND
- R114 pad 1: +3V3 -> Net-(U21-PB4)
- R114 pad 2: /Motors/ESC2/NFAULT -> DSHOT_3
- R115 pad 1: Net-(U23-DT) -> Net-(U22-VDSLVL)
- R115 pad 2: GND -> +3V3
- R116 pad 1: Net-(U22-PB4) -> GND
- R116 pad 2: DSHOT_3 -> Net-(U22-VDSLVL)
- R117 pad 1: Net-(U23-VDSLVL) -> /Motors/ESC3/VSENSE
- R117 pad 2: +3V3 -> +BATT
- R118 pad 2: Net-(U23-VDSLVL) -> /Motors/ESC3/VSENSE
- R119 pad 1: /Motors/ESC2/VSENSE -> Net-(Q17-G)
- R119 pad 2: +BATT -> /Motors/ESC3/GHA
- R120 pad 1: GND -> Net-(Q18-G)
- R120 pad 2: /Motors/ESC2/VSENSE -> /Motors/ESC3/GLA
- R121 pad 1: Net-(Q17-G) -> /Motors/ESC3/LSS
- R121 pad 2: /Motors/ESC2/GHA -> GND
- R122 pad 1: Net-(Q18-G) -> /Motors/ESC3/ISENSE
- R122 pad 2: /Motors/ESC2/GLA -> Net-(R122-Pad2)
- R124 pad 1: /Motors/ESC2/ISENSE -> Net-(Q20-G)
- R124 pad 2: Net-(R124-Pad2) -> /Motors/ESC3/GLB
- R125 pad 1: Net-(Q19-G) -> /Motors/ESC3/VSENSE_A
- R125 pad 2: /Motors/ESC2/GHB -> /Motors/ESC3/VSENSE_REF
- R126 pad 1: Net-(Q20-G) -> GND
- R126 pad 2: /Motors/ESC2/GLB -> /Motors/ESC3/VSENSE_A
- R127 pad 1: /Motors/ESC2/VSENSE_A -> /Motors/ESC3/A
- R127 pad 2: /Motors/ESC2/VSENSE_REF -> /Motors/ESC3/VSENSE_A
- R128 pad 1: GND -> /Motors/ESC3/VSENSE_B
- R128 pad 2: /Motors/ESC2/VSENSE_A -> /Motors/ESC3/VSENSE_REF
- R129 pad 1: /Motors/ESC2/A -> GND
- R129 pad 2: /Motors/ESC2/VSENSE_A -> /Motors/ESC3/VSENSE_B
- R13 pad 1: /Coprocessor/ANT_5G -> Net-(JP2-A)
- R13 pad 2: Net-(U4-P1) -> +3V3
- R130 pad 1: /Motors/ESC2/VSENSE_B -> /Motors/ESC3/B
- R130 pad 2: /Motors/ESC2/VSENSE_REF -> /Motors/ESC3/VSENSE_B
- R131 pad 1: GND -> Net-(Q21-G)
- R131 pad 2: /Motors/ESC2/VSENSE_B -> /Motors/ESC3/GHC
- R132 pad 1: /Motors/ESC2/B -> Net-(Q22-G)
- R132 pad 2: /Motors/ESC2/VSENSE_B -> /Motors/ESC3/GLC
- R133 pad 1: Net-(Q21-G) -> /Motors/ESC3/VSENSE_C
- R133 pad 2: /Motors/ESC2/GHC -> /Motors/ESC3/VSENSE_REF
- R134 pad 1: Net-(Q22-G) -> GND
- R134 pad 2: /Motors/ESC2/GLC -> /Motors/ESC3/VSENSE_C
- R135 pad 1: /Motors/ESC2/VSENSE_C -> /Motors/ESC3/C
- R135 pad 2: /Motors/ESC2/VSENSE_REF -> /Motors/ESC3/VSENSE_C
- R136 pad 1: GND -> Net-(U24-PA0)
- R136 pad 2: /Motors/ESC2/VSENSE_C -> Net-(D14-A)
- R137 pad 1: /Motors/ESC2/C -> +3V3
- R137 pad 2: /Motors/ESC2/VSENSE_C -> /Motors/ESC4/NFAULT
- R138 pad 1: Net-(U25-PA0) -> Net-(U25-DT)
- R138 pad 2: Net-(D17-A) -> GND
- R139 pad 1: +3V3 -> Net-(U24-PB4)
- R139 pad 2: /Motors/ESC3/NFAULT -> DSHOT_4
- R14 pad 1: Net-(U4-P2) -> +3V3
- R14 pad 2: /Coprocessor/ANT_2G -> CP_EN
- R140 pad 1: Net-(U26-DT) -> Net-(U25-VDSLVL)
- R140 pad 2: GND -> +3V3
- R141 pad 1: Net-(U25-PB4) -> GND
- R141 pad 2: DSHOT_4 -> Net-(U25-VDSLVL)
- R142 pad 1: Net-(U26-VDSLVL) -> /Motors/ESC4/VSENSE
- R142 pad 2: +3V3 -> +BATT
- R143 pad 2: Net-(U26-VDSLVL) -> /Motors/ESC4/VSENSE
- R144 pad 1: /Motors/ESC3/VSENSE -> Net-(Q23-G)
- R144 pad 2: +BATT -> /Motors/ESC4/GHA
- R145 pad 1: GND -> Net-(Q24-G)
- R145 pad 2: /Motors/ESC3/VSENSE -> /Motors/ESC4/GLA
- R146 pad 1: Net-(Q23-G) -> /Motors/ESC4/LSS
- R146 pad 2: /Motors/ESC3/GHA -> GND
- R147 pad 1: Net-(Q24-G) -> /Motors/ESC4/ISENSE
- R147 pad 2: /Motors/ESC3/GLA -> Net-(R147-Pad2)
- R149 pad 1: /Motors/ESC3/ISENSE -> Net-(Q26-G)
- R149 pad 2: Net-(R149-Pad2) -> /Motors/ESC4/GLB
- R15 pad 1: Net-(JP2-A) -> GND
- R15 pad 2: +3V3 -> Net-(JP2-B)
- R150 pad 1: Net-(Q25-G) -> /Motors/ESC4/VSENSE_A
- R150 pad 2: /Motors/ESC3/GHB -> /Motors/ESC4/VSENSE_REF
- R151 pad 1: Net-(Q26-G) -> GND
- R151 pad 2: /Motors/ESC3/GLB -> /Motors/ESC4/VSENSE_A
- R152 pad 1: /Motors/ESC3/VSENSE_A -> /Motors/ESC4/A
- R152 pad 2: /Motors/ESC3/VSENSE_REF -> /Motors/ESC4/VSENSE_A
- R153 pad 1: GND -> /Motors/ESC4/VSENSE_B
- R153 pad 2: /Motors/ESC3/VSENSE_A -> /Motors/ESC4/VSENSE_REF
- R154 pad 1: /Motors/ESC3/A -> GND
- R154 pad 2: /Motors/ESC3/VSENSE_A -> /Motors/ESC4/VSENSE_B
- R155 pad 1: /Motors/ESC3/VSENSE_B -> /Motors/ESC4/B
- R155 pad 2: /Motors/ESC3/VSENSE_REF -> /Motors/ESC4/VSENSE_B
- R156 pad 1: GND -> Net-(Q27-G)
- R156 pad 2: /Motors/ESC3/VSENSE_B -> /Motors/ESC4/GHC
- R157 pad 1: /Motors/ESC3/B -> Net-(Q28-G)
- R157 pad 2: /Motors/ESC3/VSENSE_B -> /Motors/ESC4/GLC
- R158 pad 1: Net-(Q27-G) -> /Motors/ESC4/VSENSE_C
- R158 pad 2: /Motors/ESC3/GHC -> /Motors/ESC4/VSENSE_REF
- R159 pad 1: Net-(Q28-G) -> GND
- R159 pad 2: /Motors/ESC3/GLC -> /Motors/ESC4/VSENSE_C
- R16 pad 1: Net-(J4-In) -> CP_SDIO_D1
- R16 pad 2: Net-(U4-P3) -> +3V3
- R160 pad 1: /Motors/ESC3/VSENSE_C -> /Motors/ESC4/C
- R160 pad 2: /Motors/ESC3/VSENSE_REF -> /Motors/ESC4/VSENSE_C
- R17 pad 1: +3V3 -> CP_SDIO_D0
- R17 pad 2: CP_EN -> +3V3
- R18 pad 1: GND -> Net-(JP6-A)
- R18 pad 2: Net-(JP2-B) -> +3V3
- R19 pad 1: CP_SDIO_D1 -> CP_SDIO_CMD
- R20 pad 1: CP_SDIO_D0 -> Net-(JP3-A)
- R20 pad 2: +3V3 -> GND
- R21 pad 1: Net-(JP6-A) -> Net-(JP4-B)
- R21 pad 2: +3V3 -> GND
- R22 pad 1: CP_SDIO_CMD -> Net-(JP5-B)
- R22 pad 2: +3V3 -> GND
- R23 pad 1: Net-(JP3-A) -> CP_SDIO_D3
- R23 pad 2: GND -> +3V3
- R24 pad 1: Net-(JP4-B) -> GND
- R24 pad 2: GND -> Net-(JP6-B)
- R25 pad 1: Net-(JP5-B) -> CP_SDIO_D2
- R25 pad 2: GND -> +3V3
- R26 pad 1: CP_SDIO_D3 -> /Coprocessor/ANT_5G
- R26 pad 2: +3V3 -> Net-(U5-P1)
- R27 pad 1: GND -> Net-(U5-P2)
- R27 pad 2: Net-(JP6-B) -> /Coprocessor/ANT_2G
- R28 pad 1: CP_SDIO_D2 -> Net-(J5-In)
- R28 pad 2: +3V3 -> Net-(U5-P3)
- R40 pad 1: /Motors/ESC/LSS -> SD_SDIO_D2
- R40 pad 2: GND -> +3V3
- R41 pad 1: /Motors/ESC1/LSS -> SD_SDIO_D3
- R41 pad 2: GND -> +3V3
- R42 pad 1: SD_SDIO_D2 -> SD_SDIO_CMD
- R43 pad 1: SD_SDIO_D3 -> SD_SDIO_D0
- R44 pad 1: SD_SDIO_CMD -> SD_SDIO_D1
- R45 pad 1: SD_SDIO_D0 -> Net-(U11-XSHUT)
- R46 pad 1: SD_SDIO_D1 -> Net-(U12-~{CS})
- R47 pad 1: Net-(U12-XSHUT) -> Net-(U13-CS)
- R48 pad 1: Net-(U13-~{CS}) -> Net-(U14-NRESET)
- R49 pad 1: Net-(U14-CS) -> I2C_SDA
- R50 pad 1: Net-(U15-NRESET) -> SPI_PMW3901_CS
- R51 pad 1: I2C_SDA -> I2C_SCL
- R52 pad 1: SPI_PMW3901_CS -> +3V3
- R52 pad 2: +3V3 -> SPI_EXT_CS
- R53 pad 1: I2C_SCL -> DC_MOT1
- R53 pad 2: +3V3 -> Net-(Q1-G)
- R54 pad 1: +3V3 -> DC_MOT3
- R54 pad 2: SPI_EXT_CS -> Net-(Q2-G)
- R55 pad 1: DC_MOT1 -> Net-(Q1-G)
- R55 pad 2: Net-(Q1-G) -> GND
- R56 pad 1: DC_MOT3 -> Net-(Q2-G)
- R56 pad 2: Net-(Q2-G) -> GND
- R57 pad 1: Net-(Q1-G) -> DC_MOT2
- R57 pad 2: GND -> Net-(Q3-G)
- R58 pad 1: Net-(Q2-G) -> DC_MOT4
- R58 pad 2: GND -> Net-(Q4-G)
- R59 pad 1: DC_MOT2 -> Net-(Q3-G)
- R59 pad 2: Net-(Q3-G) -> GND
- R60 pad 1: DC_MOT4 -> Net-(Q4-G)
- R60 pad 2: Net-(Q4-G) -> GND
- R61 pad 1: Net-(Q3-G) -> Net-(U15-PA0)
- R61 pad 2: GND -> Net-(D11-A)
- R62 pad 1: Net-(Q4-G) -> +3V3
- R62 pad 2: GND -> /Motors/ESC1/NFAULT
- R63 pad 1: Net-(U16-PA0) -> Net-(U16-DT)
- R63 pad 2: Net-(D11-A) -> GND
- R64 pad 1: +3V3 -> Net-(U15-PB4)
- R64 pad 2: /Motors/ESC/NFAULT -> DSHOT_1
- R65 pad 1: Net-(U17-DT) -> Net-(U16-VDSLVL)
- R65 pad 2: GND -> +3V3
- R66 pad 1: Net-(U16-PB4) -> GND
- R66 pad 2: DSHOT_1 -> Net-(U16-VDSLVL)
- R67 pad 1: Net-(U17-VDSLVL) -> /Motors/ESC1/VSENSE
- R67 pad 2: +3V3 -> +BATT
- R68 pad 2: Net-(U17-VDSLVL) -> /Motors/ESC1/VSENSE
- R69 pad 1: /Motors/ESC/VSENSE -> Net-(Q5-G)
- R69 pad 2: +BATT -> /Motors/ESC1/GHA
- R70 pad 1: GND -> Net-(Q6-G)
- R70 pad 2: /Motors/ESC/VSENSE -> /Motors/ESC1/GLA
- R71 pad 1: Net-(Q5-G) -> /Motors/ESC1/LSS
- R71 pad 2: /Motors/ESC/GHA -> GND
- R72 pad 1: Net-(Q6-G) -> /Motors/ESC1/ISENSE
- R72 pad 2: /Motors/ESC/GLA -> Net-(R72-Pad2)
- R74 pad 1: /Motors/ESC/ISENSE -> Net-(Q8-G)
- R74 pad 2: Net-(R74-Pad2) -> /Motors/ESC1/GLB
- R75 pad 1: Net-(Q7-G) -> /Motors/ESC1/VSENSE_A
- R75 pad 2: /Motors/ESC/GHB -> /Motors/ESC1/VSENSE_REF
- R76 pad 1: Net-(Q8-G) -> GND
- R76 pad 2: /Motors/ESC/GLB -> /Motors/ESC1/VSENSE_A
- R77 pad 1: /Motors/ESC/VSENSE_A -> /Motors/ESC1/A
- R77 pad 2: /Motors/ESC/VSENSE_REF -> /Motors/ESC1/VSENSE_A
- R78 pad 1: GND -> /Motors/ESC1/VSENSE_B
- R78 pad 2: /Motors/ESC/VSENSE_A -> /Motors/ESC1/VSENSE_REF
- R79 pad 1: /Motors/ESC/A -> GND
- R79 pad 2: /Motors/ESC/VSENSE_A -> /Motors/ESC1/VSENSE_B
- R8 pad 1: Net-(J2-Pin_1) -> Net-(J2-Pin_3)
- R80 pad 1: /Motors/ESC/VSENSE_B -> /Motors/ESC1/B
- R80 pad 2: /Motors/ESC/VSENSE_REF -> /Motors/ESC1/VSENSE_B
- R81 pad 1: GND -> Net-(Q9-G)
- R81 pad 2: /Motors/ESC/VSENSE_B -> /Motors/ESC1/GHC
- R82 pad 1: /Motors/ESC/B -> Net-(Q10-G)
- R82 pad 2: /Motors/ESC/VSENSE_B -> /Motors/ESC1/GLC
- R83 pad 1: Net-(Q9-G) -> /Motors/ESC1/VSENSE_C
- R83 pad 2: /Motors/ESC/GHC -> /Motors/ESC1/VSENSE_REF
- R84 pad 1: Net-(Q10-G) -> GND
- R84 pad 2: /Motors/ESC/GLC -> /Motors/ESC1/VSENSE_C
- R85 pad 1: /Motors/ESC/VSENSE_C -> /Motors/ESC1/C
- R85 pad 2: /Motors/ESC/VSENSE_REF -> /Motors/ESC1/VSENSE_C
- R86 pad 1: GND -> Net-(U18-PA0)
- R86 pad 2: /Motors/ESC/VSENSE_C -> Net-(D12-A)
- R87 pad 1: /Motors/ESC/C -> +3V3
- R87 pad 2: /Motors/ESC/VSENSE_C -> /Motors/ESC2/NFAULT
- R88 pad 1: Net-(U19-PA0) -> Net-(U19-DT)
- R88 pad 2: Net-(D13-A) -> GND
- R89 pad 1: +3V3 -> Net-(U18-PB4)
- R89 pad 2: /Motors/ESC1/NFAULT -> DSHOT_2
- R90 pad 1: Net-(U20-DT) -> Net-(U19-VDSLVL)
- R90 pad 2: GND -> +3V3
- R91 pad 1: Net-(U19-PB4) -> GND
- R91 pad 2: DSHOT_2 -> Net-(U19-VDSLVL)
- R92 pad 1: Net-(U20-VDSLVL) -> /Motors/ESC2/VSENSE
- R92 pad 2: +3V3 -> +BATT
- R93 pad 2: Net-(U20-VDSLVL) -> /Motors/ESC2/VSENSE
- R94 pad 1: /Motors/ESC1/VSENSE -> Net-(Q11-G)
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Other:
- board size 55 x 55 mm -> 60 x 60 mm
